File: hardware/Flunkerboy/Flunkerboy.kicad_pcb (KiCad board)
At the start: 2 copper layers, 51 x 60.4 mm, 23 parts, among them J1 GameBoy_GamePak_DMG-09, J2 Conn_01x01_Socket, J3 Conn_01x01_Socket, U1 74LS574, U2 74LS04, U5 AD9283, U6 OPA2333AIDR(UMW), U7 CD4051B

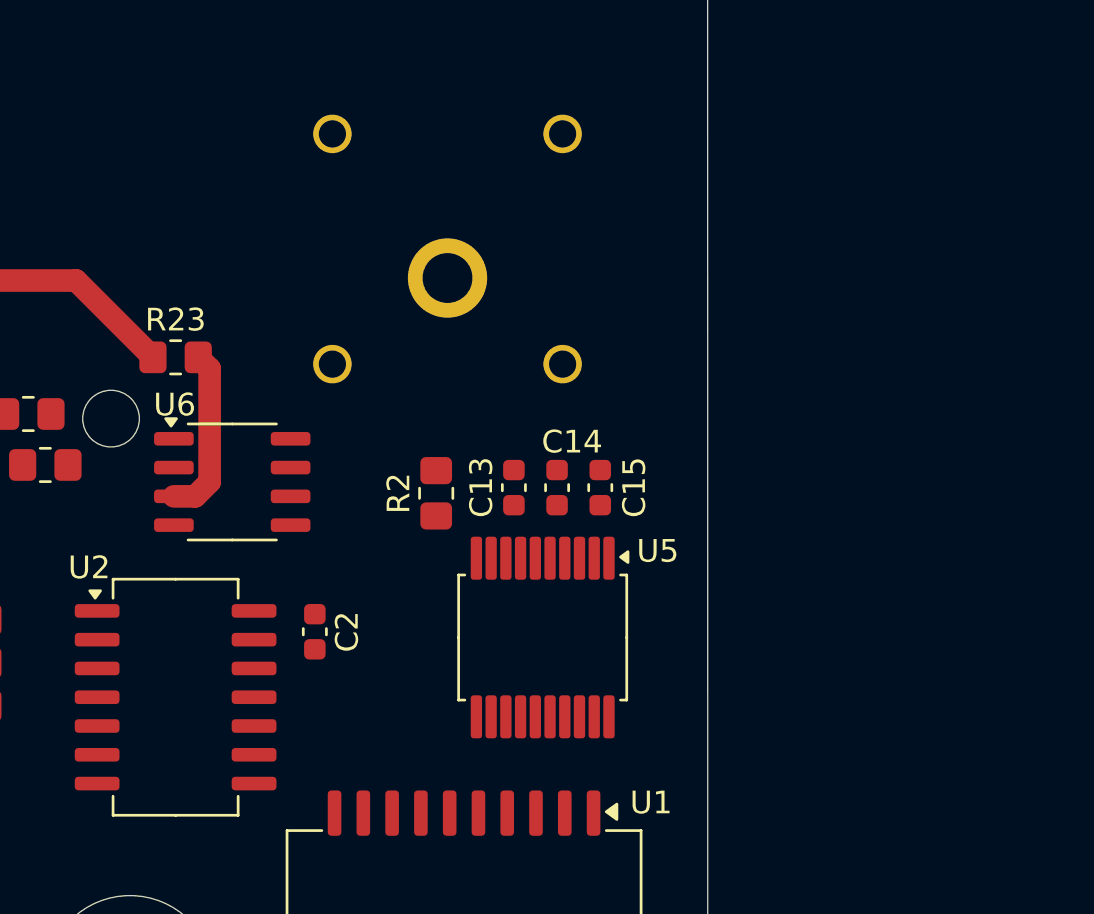
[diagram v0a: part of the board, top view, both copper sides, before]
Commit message: add mosfets
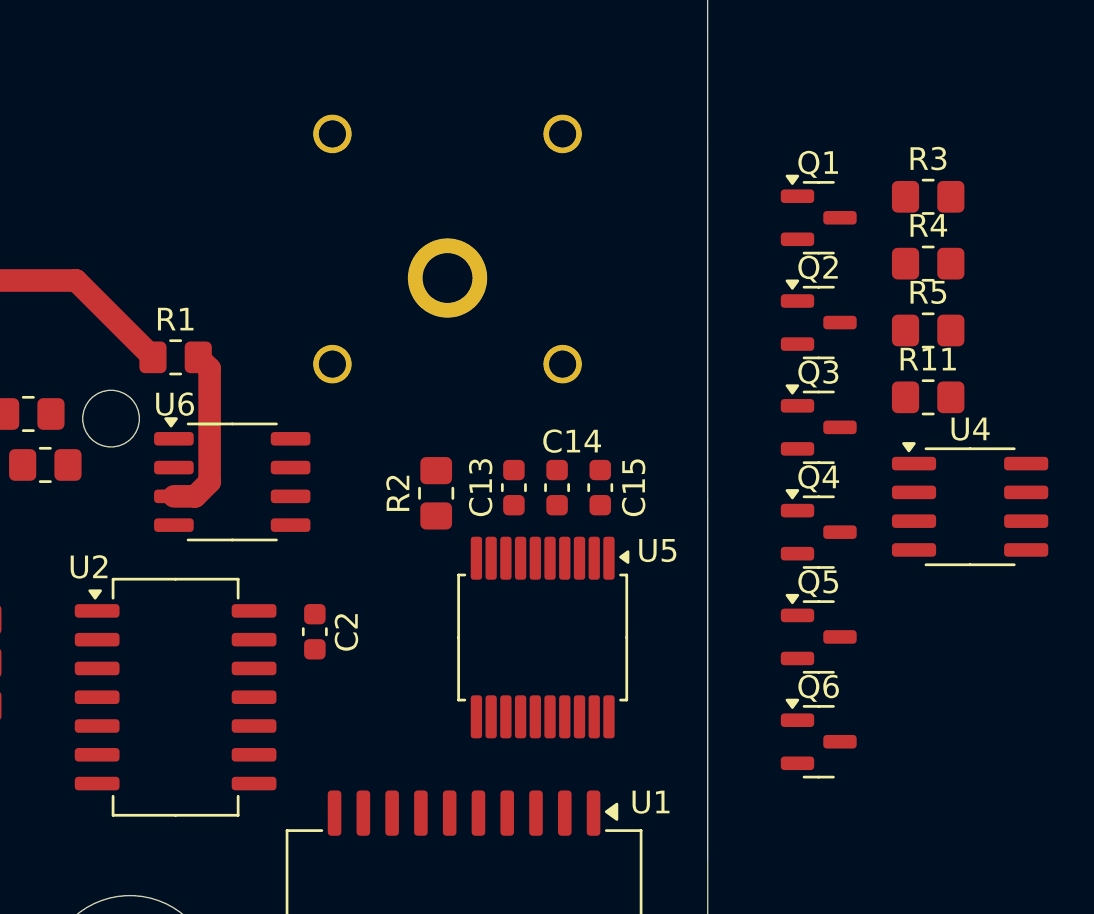
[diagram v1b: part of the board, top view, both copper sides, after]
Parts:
- added Q1: AO3400A, Package_TO_SOT_SMD:SOT-23, F.Cu at (129.6, 83.1)
- added Q2: AO3400A, Package_TO_SOT_SMD:SOT-23, F.Cu at (129.6, 87.7)
- added Q3: AO3400A, Package_TO_SOT_SMD:SOT-23, F.Cu at (129.6, 92.3)
- added Q4: AO3400A, Package_TO_SOT_SMD:SOT-23, F.Cu at (129.6, 97.0)
- added Q5: AO3400A, Package_TO_SOT_SMD:SOT-23, F.Cu at (129.6, 101.6)
- added Q6: AO3400A, Package_TO_SOT_SMD:SOT-23, F.Cu at (129.6, 106.2)
- added R11: 235k, Resistor_SMD:R_0805_2012Metric_Pad1.20x1.40mm_HandSolder, F.Cu at (134.4, 91.0)
- added R3: 235k, Resistor_SMD:R_0805_2012Metric_Pad1.20x1.40mm_HandSolder, F.Cu at (134.4, 82.2)
- added R4: 235k, Resistor_SMD:R_0805_2012Metric_Pad1.20x1.40mm_HandSolder, F.Cu at (134.4, 85.1)
- added R5: 235k, Resistor_SMD:R_0805_2012Metric_Pad1.20x1.40mm_HandSolder, F.Cu at (134.4, 88.1)
- added U4: OPA356xxD, Package_SO:SOIC-8_3.9x4.9mm_P1.27mm, F.Cu at (136.3, 95.8)
- R25: value 56k -> 55k
- renumbered R23 to R1
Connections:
- R1 pad 1: Net-(J2-Pin_1) -> /Vmes
- R1 pad 2: Net-(U6A-+) -> GND
- R10 pad 1: GND -> /Vmes
- R10 pad 2: Net-(U7-X5) -> Net-(Q6-S)
- R24 pad 2: Net-(U6A--) -> Net-(R11-Pad1)
- R25 pad 1: Net-(U6A--) -> Net-(R11-Pad1)
- R6 pad 1: GND -> /Vmes
- R6 pad 2: Net-(U7-X1) -> Net-(Q2-S)
- R7 pad 1: GND -> /Vmes
- R7 pad 2: Net-(U7-X2) -> Net-(Q3-S)
- R8 pad 1: GND -> /Vmes
- R8 pad 2: Net-(U7-X3) -> Net-(Q4-S)
- R9 pad 1: GND -> /Vmes
- R9 pad 2: Net-(U7-X4) -> Net-(Q5-S)
- U5 pad 5: +3.3V -> unconnected-(U5-VaD-Pad5)
- U5 pad 7: Ain -> unconnected-(U5-Ain+-Pad7)
- U5 pad 8: +3.3V -> unconnected-(U5-VaD-Pad8)
- U7 pad 1: Net-(U7-X4) -> Net-(Q5-G)
- U7 pad 12: Net-(U7-X3) -> Net-(Q4-G)
- U7 pad 13: GND -> Net-(Q1-G)
- U7 pad 14: Net-(U7-X1) -> /Vmes
- U7 pad 15: Net-(U7-X2) -> Net-(Q3-G)
- U7 pad 3: Net-(U6A-+) -> +3.3V
- U7 pad 5: Net-(U7-X5) -> Net-(Q6-G)

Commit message: build imput devider
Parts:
- removed Q1, Q2, Q3, Q4, Q5, Q6: AO3400A, Package_TO_SOT_SMD:SOT-23
- removed R9: 115k, Resistor_SMD:R_0805_2012Metric_Pad1.20x1.40mm_HandSolder
- removed U2: 74LS04, Package_SO:SO-14_5.3x10.2mm_P1.27mm
- added C10: C, Capacitor_SMD:C_0805_2012Metric, F.Cu at (167.2, 86.4)
- added C11: C, Capacitor_SMD:C_0805_2012Metric, F.Cu at (167.2, 89.5)
- added C16: 100n, Capacitor_SMD:C_0805_2012Metric, F.Cu at (167.2, 95.5)
- added C17: 100n, Capacitor_SMD:C_0805_2012Metric, F.Cu at (171.6, 86.4)
- added C18: 100n, Capacitor_SMD:C_0805_2012Metric, F.Cu at (171.6, 89.5)
- added C19: 100n, Capacitor_SMD:C_0805_2012Metric, F.Cu at (171.6, 92.5)
- added C20: 100n, Capacitor_SMD:C_0805_2012Metric, F.Cu at (171.6, 95.5)
- added C3: 100n, Capacitor_SMD:C_0805_2012Metric, F.Cu at (158.3, 89.5)
- added C4: 100n, Capacitor_SMD:C_0805_2012Metric, F.Cu at (158.3, 92.5)
- added C5: 100n, Capacitor_SMD:C_0805_2012Metric, F.Cu at (158.3, 95.5)
- added C6: 100n, Capacitor_SMD:C_0805_2012Metric, F.Cu at (162.7, 86.4)
- added C7: 100n, Capacitor_SMD:C_0805_2012Metric, F.Cu at (162.7, 89.5)
- added C8: 100n, Capacitor_SMD:C_0805_2012Metric, F.Cu at (162.7, 92.5)
- added C9: 100n, Capacitor_SMD:C_0805_2012Metric, F.Cu at (162.7, 95.5)
- added D1: 1N4007, Diode_SMD:D_SOD-123F, F.Cu at (158.8, 102.9)
- added D10: LM385, Package_TO_SOT_SMD:SOT-23, F.Cu at (145.3, 114.7)
- added D1a1: 1N4007, Diode_SMD:D_SOD-123F, F.Cu at (158.8, 109.6)
- added D2: 1N4007, Diode_SMD:D_SOD-123F, F.Cu at (158.8, 106.2)
- added D2a1: 1N4007, Diode_SMD:D_SOD-123F, F.Cu at (158.8, 113.0)
- added D3: 3.3V, Diode_SMD:D_SOD-123, F.Cu at (145.7, 107.3)
- added D4: 1V, Diode_SMD:D_SOD-123F, F.Cu at (196.2, 84.9)
- added D6: 8.2V 1.3W, Diode_SMD:D_SMB, F.Cu at (165.7, 104.0)
- added D7: 8,2V 1,3W, Diode_SMD:D_SMB, F.Cu at (165.7, 109.5)
- added D8: DX400, Diode_SMD:D_SOD-123, F.Cu at (151.1, 110.8)
- added D9: DX400, Diode_SMD:D_SOD-123, F.Cu at (145.7, 110.6)
- added F1: 2A, MyLibrary:2410, F.Cu at (166.3, 114.2)
- added F2: 50mA, Resistor_SMD:R_0805_2012Metric, F.Cu at (145.0, 86.4)
- added F3: 50mA, Resistor_SMD:R_0805_2012Metric, F.Cu at (145.0, 89.4)
- added K1: AGQ200A4HZ, Relay_THT:Relay_DPDT_Omron_G6K-2P-Y, F.Cu at (135.3, 75.4)
- added K2: AGQ200A4HZ, Relay_THT:Relay_DPDT_Omron_G6K-2P-Y, F.Cu at (143.7, 75.4)
- added K3: AGQ200A4HZ, Relay_THT:Relay_DPDT_Omron_G6K-2P-Y, F.Cu at (152.1, 75.4)
- added K4: AGQ200A4HZ, Relay_THT:Relay_DPDT_Omron_G6K-2P-Y, F.Cu at (160.4, 75.4)
- added R12: 235k, Resistor_SMD:R_0805_2012Metric_Pad1.20x1.40mm_HandSolder, F.Cu at (178.2, 80.6)
- added R13: 235k, Resistor_SMD:R_0805_2012Metric_Pad1.20x1.40mm_HandSolder, F.Cu at (178.2, 83.5)
- added R14: 25, Resistor_SMD:R_0805_2012Metric_Pad1.20x1.40mm_HandSolder, F.Cu at (178.2, 86.5)
- added R37: 2k2, Resistor_SMD:R_0805_2012Metric, F.Cu at (149.4, 95.3)
- added R39: 15k, Resistor_SMD:R_0805_2012Metric, F.Cu at (149.4, 98.2)
- added R40: 2k2, Resistor_SMD:R_0805_2012Metric, F.Cu at (149.4, 101.2)
- added R42: 10k, Resistor_SMD:R_0805_2012Metric, F.Cu at (149.4, 104.1)
- added R46: 100, Resistor_SMD:R_0805_2012Metric, F.Cu at (153.8, 86.4)
- added R47: 1k, Resistor_SMD:R_0805_2012Metric, F.Cu at (153.8, 89.4)
- added R63: 1k, Resistor_SMD:R_0805_2012Metric, F.Cu at (153.8, 92.3)
- added RV41: 100k, Resistor_SMD:R_0805_2012Metric, F.Cu at (153.8, 95.3)
- added U13: AD9283, Package_SO:SSOP-20_5.3x7.2mm_P0.65mm, F.Cu at (185.8, 94.5)
- added U14: 74LS574, Package_SO:SOIC-20W_7.5x15.4mm_P1.27mm, F.Cu at (187.0, 81.7)
- added U8: ADG1611, Package_SO:TSSOP-16_4.4x5mm_P0.65mm, F.Cu at (138.4, 114.6)
- C12, C2: footprint Capacitor_SMD:C_0603_1608Metric -> Capacitor_SMD:C_0805_2012Metric
- J2, J3: moved to F.Cu
- R1: value 5k -> 900k; footprint Resistor_SMD:R_0805_2012Metric_Pad1.20x1.40mm_HandSolder -> Resistor_SMD:R_0805_2012Metric
- R2: value 25 -> 90k; footprint Resistor_SMD:R_0805_2012Metric_Pad1.20x1.40mm_HandSolder -> Resistor_SMD:R_0805_2012Metric
- R3: value 235k -> 9k; footprint Resistor_SMD:R_0805_2012Metric_Pad1.20x1.40mm_HandSolder -> Resistor_SMD:R_0805_2012Metric
- R4: value 235k -> 900; footprint Resistor_SMD:R_0805_2012Metric_Pad1.20x1.40mm_HandSolder -> Resistor_SMD:R_0805_2012Metric
- R5: value 235k -> 90; footprint Resistor_SMD:R_0805_2012Metric_Pad1.20x1.40mm_HandSolder -> Resistor_SMD:R_0805_2012Metric
- R6: value 10k -> 9; footprint Resistor_SMD:R_0805_2012Metric_Pad1.20x1.40mm_HandSolder -> Resistor_SMD:R_0805_2012Metric
- R7: value 25k -> 0.9; footprint Resistor_SMD:R_0805_2012Metric_Pad1.20x1.40mm_HandSolder -> Resistor_SMD:R_0805_2012Metric
- R8: value 55k -> 0.1; footprint Resistor_SMD:R_0805_2012Metric_Pad1.20x1.40mm_HandSolder -> Resistor_SMD:R_0805_2012Metric
- U1: value 74LS574 -> OPA356xxD; footprint Package_SO:SOIC-20W_7.5x15.4mm_P1.27mm -> Package_SO:SOIC-8_3.9x4.9mm_P1.27mm
- U4: value OPA356xxD -> ADG1611; footprint Package_SO:SOIC-8_3.9x4.9mm_P1.27mm -> Package_SO:TSSOP-16_4.4x5mm_P0.65mm
- U5: value AD9283 -> ADG1611; footprint Package_SO:SSOP-20_5.3x7.2mm_P0.65mm -> Package_SO:TSSOP-16_4.4x5mm_P0.65mm
- U6: value OPA2333AIDR(UMW) -> ADG1611; footprint Package_SO:SO-8_3.9x4.9mm_P1.27mm -> Package_SO:TSSOP-16_4.4x5mm_P0.65mm
- U7: value CD4051B -> ADG1611; footprint Package_SO:SO-16_3.9x9.9mm_P1.27mm -> Package_SO:TSSOP-16_4.4x5mm_P0.65mm
- moved R10 102.4 mm to (178.2, 74.7)
- moved C1 85.8 mm to (195.4, 74.5)
- moved U1 83.9 mm to (195.3, 93.5), turned to 0 degrees
- moved R25 83.5 mm to (178.2, 92.4)
- moved R24 82.9 mm to (178.2, 89.4)
- moved C13 81.3 mm to (195.4, 77.0), turned to 0 degrees
- moved C14 78.9 mm to (195.4, 79.5), turned to 0 degrees
- moved C12 78.5 mm to (167.2, 92.5), turned to 0 degrees
- moved C15 76.6 mm to (195.4, 82.0), turned to 0 degrees
- moved R6 59.8 mm to (149.4, 86.4), turned to 0 degrees
- moved R8 58.8 mm to (149.4, 92.3), turned to 0 degrees
- moved R7 58.6 mm to (149.4, 89.4), turned to 0 degrees
- moved C2 53.0 mm to (158.3, 86.4), turned to 0 degrees
- moved U7 52.4 mm to (138.4, 108.0)
- moved R11 45.8 mm to (178.2, 77.6)
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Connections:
- net /SW3 renamed /Eingangsteiler/S10b
- net Ain renamed /Eingangsteiler/S8b
- C12 pad 1: +3.3V -> Net-(D3-K)
- C12 pad 2: GND -> /Eingangsteiler/D
- C13 pad 1: Net-(U5-Ain-) -> Net-(U13-Ain-)
- C15 pad 1: Net-(U5-VREFin) -> Net-(U13-VREFin)
- C2 pad 1: +3.3V -> -3V3
- J3 pad 1: GND -> GNDA
- R1 pad 1: /Vmes -> Net-(U5C-S3)
- R1 pad 2: GND -> Net-(U6C-S3)
- R10 pad 2: Net-(Q6-S) -> Net-(U1-+)
- R11 pad 2: Net-(U4--) -> Net-(U1--)
- R2 pad 1: Net-(U5-Ain-) -> Net-(U6C-S3)
- R2 pad 2: GND -> Net-(U4C-S3)
- R3 pad 1: Net-(U4-+) -> Net-(U4C-S3)
- R3 pad 2: GND -> Net-(U5B-S2)
- R4 pad 1: /Vmes -> Net-(U5B-S2)
- R4 pad 2: Net-(U4-+) -> Net-(U5A-S1)
- R5 pad 1: Net-(U4--) -> Net-(U5A-S1)
- R5 pad 2: Net-(R5-Pad2) -> Net-(U4B-S2)
- R6 pad 1: /Vmes -> Net-(U4B-S2)
- R6 pad 2: Net-(Q2-S) -> Net-(U4D-S4)
- R7 pad 1: /Vmes -> Net-(U4D-S4)
- R7 pad 2: Net-(Q3-S) -> Net-(U8B-S2)
- R8 pad 1: /Vmes -> Net-(U8B-S2)
- R8 pad 2: Net-(Q4-S) -> GNDA
- U1 pad 1: GND -> unconnected-(U1-NC-Pad1)
- U1 pad 2: Net-(U1-D0) -> Net-(U1--)
- U1 pad 3: Net-(U1-D1) -> Net-(U1-+)
- U1 pad 4: Net-(U1-D2) -> -3V3
- U1 pad 5: Net-(U1-D3) -> unconnected-(U1-NC-Pad5)
- U1 pad 6: Net-(U1-D4) -> Net-(R13-Pad2)
- U1 pad 7: Net-(U1-D5) -> +3.3V
- U1 pad 8: Net-(U1-D6) -> unconnected-(U1-NC-Pad8)
- U4 pad 1: unconnected-(U4-NC-Pad1) -> /Eingangsteiler/S6a
- U4 pad 2: Net-(U4--) -> Net-(D6-K)
- U4 pad 3: Net-(U4-+) -> Net-(U4A-S1)
- U4 pad 5: unconnected-(U4-NC-Pad5) -> GND
- U4 pad 6: Net-(R5-Pad2) -> Net-(U4D-S4)
- U4 pad 7: +3.3V -> Net-(U4D-D4)
- U4 pad 8: unconnected-(U4-NC-Pad8) -> /Eingangsteiler/S6e
- U5 pad 1: GND -> /Eingangsteiler/S7b
- U5 pad 10: /CLKadc -> Net-(U5C-D3)
- U5 pad 11: Net-(U1-D7) -> Net-(U5C-S3)
- U5 pad 12: Net-(U1-D6) -> unconnected-(U5E-NC-Pad12)
- U5 pad 13: Net-(U1-D5) -> +3V3
- U5 pad 14: Net-(U1-D4) -> Net-(U5B-S2)
- U5 pad 15: +3.3V -> Net-(D1-A)
- U5 pad 16: GND -> /Eingangsteiler/S7d
- U5 pad 2: Net-(U5-VREFin) -> Net-(U4B-D2)
- U5 pad 3: Net-(U5-VREFin) -> Net-(U5A-S1)
- U5 pad 4: GND -> -3V3
- U5 pad 5: unconnected-(U5-VaD-Pad5) -> GND
- U5 pad 6: Net-(U5-Ain-) -> Net-(U4A-S1)
- U5 pad 7: unconnected-(U5-Ain+-Pad7) -> Net-(D6-K)
- U5 pad 8: unconnected-(U5-VaD-Pad8) -> /Eingangsteiler/S7f
- U5 pad 9: GND -> /Eingangsteiler/S7e
- U6 pad 2: Net-(U6A--) -> Net-(U4B-D2)
- U6 pad 3: Net-(U6A-+) -> Net-(U5B-S2)
- U6 pad 4: (no net) -> -3V3
- U6 pad 5: (no net) -> GND
- U6 pad 6: (no net) -> Net-(U4C-S3)
- U6 pad 7: (no net) -> Net-(U4B-D2)
- U6 pad 8: (no net) -> /Eingangsteiler/S9b
- U7 pad 1: Net-(Q5-G) -> /Eingangsteiler/S9d
- U7 pad 10: /SW2 -> Net-(U4B-D2)
- U7 pad 11: /SW1 -> Net-(U6C-S3)
- U7 pad 12: Net-(Q4-G) -> unconnected-(U7E-NC-Pad12)
- U7 pad 13: Net-(Q1-G) -> +3V3
- U7 pad 14: /Vmes -> Net-(U4C-S3)
- U7 pad 15: Net-(Q3-G) -> Net-(U5C-D3)
- U7 pad 16: +3.3V -> /Eingangsteiler/S9e
- U7 pad 2: unconnected-(U7-X6-Pad2) -> Net-(D1-A)
- U7 pad 3: +3.3V -> Net-(U4B-S2)
- U7 pad 4: unconnected-(U7-X7-Pad4) -> -3V3
- U7 pad 5: Net-(Q6-G) -> GND
- U7 pad 6: GND -> Net-(U4D-S4)
- U7 pad 7: GND -> Net-(D1-A)
- U7 pad 8: GND -> /Eingangsteiler/S10d
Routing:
- net Net-(J2-Pin_1): track 16.4 -> 0.00 mm
- net Net-(U6A-+): track 7.55 -> 0.00 mm
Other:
- outline, holes or cut-outs redrawn
- board text added: "32"

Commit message: add docs
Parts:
- removed C17, C18, C19, C20: 100n, Capacitor_SMD:C_0805_2012Metric
- removed K1, K2, K3, K4: AGQ200A4HZ, Relay_THT:Relay_DPDT_Omron_G6K-2P-Y
- added D11: 1N4148, Diode_SMD:D_SOD-123, F.Cu at (77.6, 73.2)
- added D12: 1N4148, Diode_SMD:D_SOD-123, F.Cu at (120.6, 73.5)
- added D13: 1N4148, Diode_SMD:D_SOD-123, F.Cu at (114.3, 94.7)
- added D5: 1N4148, Diode_SMD:D_SOD-123, F.Cu at (76.2, 96.9)
- added RL1: AGQ200A4HZ, Relay_THT:Relay_DPDT_Omron_G6K-2P-Y, F.Cu at (80.3, 94.1)
- added RL3: AGQ200A4HZ, Relay_THT:Relay_DPDT_Omron_G6K-2P-Y, F.Cu at (123.2, 94.7)
- added RL4: AGQ200A4HZ, Relay_THT:Relay_DPDT_Omron_G6K-2P-Y, F.Cu at (118.1, 76.5)
- added RL6: AGQ200A4HZ, Relay_THT:Relay_DPDT_Omron_G6K-2P-Y, F.Cu at (74.9, 75.8)
- RV41: footprint Resistor_SMD:R_0805_2012Metric -> Potentiometer_SMD:Potentiometer_Bourns_3224J_Horizontal
- moved C16 112.5 mm to (56.9, 117.5)
- moved RV41 99.0 mm to (56.4, 113.2)
- moved R40 98.8 mm to (51.1, 111.3)
- moved D8 97.2 mm to (54.1, 105.0)
- moved F2 95.9 mm to (51.4, 107.2)
- moved C15 94.9 mm to (103.1, 104.3)
- moved C13 94.1 mm to (104.1, 99.5)
- moved D10 94.0 mm to (51.2, 115.2)
- moved R39 87.1 mm to (63.2, 111.0)
- moved R42 87.1 mm to (63.2, 117.0)
- moved C2 87.1 mm to (103.2, 153.9)
- moved C3 87.1 mm to (103.2, 156.9)
- moved D9 86.2 mm to (59.8, 104.8)
- moved D4 86.1 mm to (110.9, 97.5), turned to 180 degrees
- moved C1 84.1 mm to (122.2, 116.0)
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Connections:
- R13 pad 2: Net-(R13-Pad2) -> Net-(U13-Ain+)
- U1 pad 6: Net-(R13-Pad2) -> Net-(U13-Ain+)
- U13 pad 7: unconnected-(U13-Ain+-Pad7) -> Net-(U13-Ain+)
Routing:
- added copper zone on B.Cu, net GND
- added copper zone on F.Cu, net GND

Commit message: add 3D files
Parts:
- moved U8 4.74 mm to (94.5, 95.7)
- moved C12 3.75 mm to (95.7, 90.7), turned to 0 degrees
- moved R37 1.76 mm to (95.0, 87.9)
- moved C11 0.95 mm to (98.4, 99.6), turned to 90 degrees
- moved D3 0.37 mm to (92.7, 88.6)
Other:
- outline, holes or cut-outs redrawn
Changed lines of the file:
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@@
 	(footprint "Capacitor_SMD:C_0805_2012Metric"
 		(layer "F.Cu")
-		(at 97.45 99.5825 -90)
+		(at 98.4 99.6 90)
 		(descr "Capacitor SMD 0805 (2012 Metric), square (rectangular) end terminal, IPC-7351 nominal, (Body size source: IPC-SM-782 page 76, https://www.pcb-3d.com/wordpress/wp-content/uploads/ipc-sm-782a_amendment_1_and_2.pdf, https://docs.google.com/spreadsheets/d/1BsfQQcO9C6DZCsRaXUlFlo91Tg2WpOkGARC1WS5S8t0/edit?usp=sharing), generated with kicad-footprint-generator")
 		(tags "capacitor")
@@
 		(attr smd)
 		(fp_line
-			(start -0.261253 0.735)
-			(end 0.261253 0.735)
+			(start -0.261253 -0.735)
+			(end 0.261253 -0.735)
 			(stroke
 				(width 0.12)
@@
 		)
 		(fp_line
-			(start -0.261253 -0.735)
-			(end 0.261253 -0.735)
+			(start -0.261253 0.735)
+			(end 0.261253 0.735)
 			(stroke
 				(width 0.12)
@@
 		)
 		(fp_line
-			(start -1.7 0.98)
-			(end -1.7 -0.98)
+			(start 1.7 -0.98)
+			(end 1.7 0.98)
 			(stroke
 				(width 0.05)
@@
 		)
 		(fp_line
-			(start 1.7 0.98)
-			(end -1.7 0.98)
+			(start -1.7 -0.98)
+			(end 1.7 -0.98)
 			(stroke
 				(width 0.05)
@@
 		)
 		(fp_line
-			(start -1.7 -0.98)
-			(end 1.7 -0.98)
+			(start 1.7 0.98)
+			(end -1.7 0.98)
 			(stroke
 				(width 0.05)
@@
 		)
 		(fp_line
-			(start 1.7 -0.98)
-			(end 1.7 0.98)
+			(start -1.7 0.98)
+			(end -1.7 -0.98)
 			(stroke
 				(width 0.05)
@@
 		)
 		(fp_line
-			(start -1 0.625)
-			(end -1 -0.625)
+			(start 1 -0.625)
+			(end 1 0.625)
 			(stroke
 				(width 0.1)
@@
 		)
 		(fp_line
-			(start 1 0.625)
-			(end -1 0.625)
+			(start -1 -0.625)
+			(end 1 -0.625)
 			(stroke
 				(width 0.1)
@@
 		)
 		(fp_line
-			(start -1 -0.625)
-			(end 1 -0.625)
+			(start 1 0.625)
+			(end -1 0.625)
 			(stroke
 				(width 0.1)
@@
 		)
 		(fp_line
-			(start 1 -0.625)
-			(end 1 0.625)
+			(start -1 0.625)
+			(end -1 -0.625)
 			(stroke
 				(width 0.1)
@@
 		)
 		(pad "1" smd roundrect
-			(at -0.949999 0 270)
+			(at -0.949999 0 90)
 			(size 1 1.45)
 			(layers "F.Cu" "F.Mask" "F.Paste")
@@
 		)
 		(pad "2" smd roundrect
-			(at 0.949999 0 270)
+			(at 0.949999 0 90)
 			(size 1 1.45)
 			(layers "F.Cu" "F.Mask" "F.Paste")
@@
 	(footprint "Package_SO:TSSOP-16_4.4x5mm_P0.65mm"
 		(layer "F.Cu")
-		(at 98.775 93.6375 -90)
+		(at 94.5 95.6875 -90)
 		(descr "TSSOP, 16 Pin (https://www.jedec.org/document_search?search_api_views_fulltext=MO-153), generated with kicad-footprint-generator ipc_gullwing_generator.py")
 		(tags "TSSOP SO JEDEC-MO-153-AB Texas_PW0016A Microchip-ST Toshiba-TSSOP16-P-0044-0.65A NXP-SOT403-1 Infineon-P-TSSOP-16-800")
@@
 		)
 		(embedded_fonts no)
+		(model "/home/jsc69/Dokumente/projekte/ComponentTester/3d/cartridge-back.step"
+			(offset
+				(xyz -29.5 -1 -3)
+			)
+			(scale
+				(xyz 1 1 1)
+			)
+			(rotate
+				(xyz -0 -0 -0)
+			)
+		)
+		(model "/home/jsc69/Dokumente/projekte/ComponentTester/3d/cartridge-front.step"
+			(hide yes)
+			(offset
+				(xyz -29.5 -1 4)
+			)
+			(scale
+				(xyz 1 1 1)
+			)
+			(rotate
+				(xyz -0 -180 -0)
+			)
+		)
 	)
 	(footprint "MyLibrary:2410"
@@
 	(footprint "Capacitor_SMD:C_0805_2012Metric"
 		(layer "F.Cu")
-		(at 92.868 93.16 -90)
+		(at 95.7 90.7)
 		(descr "Capacitor SMD 0805 (2012 Metric), square (rectangular) end terminal, IPC-7351 nominal, (Body size source: IPC-SM-782 page 76, https://www.pcb-3d.com/wordpress/wp-content/uploads/ipc-sm-782a_amendment_1_and_2.pdf, https://docs.google.com/spreadsheets/d/1BsfQQcO9C6DZCsRaXUlFlo91Tg2WpOkGARC1WS5S8t0/edit?usp=sharing), generated with kicad-footprint-generator")
 		(tags "capacitor")
 		(property "Reference" "C12"
-			(at 0 -1.679999 90)
+			(at 0 -1.679999 0)
 			(layer "F.SilkS")
 			(effects
@@
 		)
 		(property "Value" "100n"
-			(at 0 1.679999 90)
+			(at 0 1.679999 0)
 			(layer "F.Fab")
 			(effects
@@
 		)
 		(property "Datasheet" "~"
-			(at 0 0 90)
+			(at 0 0 0)
 			(layer "F.Fab")
 			(hide yes)
@@
 		)
 		(property "Description" "Unpolarized capacitor"
-			(at 0 0 90)
+			(at 0 0 0)
 			(layer "F.Fab")
 			(hide yes)
@@
 		(attr smd)
 		(fp_line
-			(start -0.261253 0.735)
-			(end 0.261253 0.735)
+			(start -0.261253 -0.735)
+			(end 0.261253 -0.735)
 			(stroke
 				(width 0.12)
@@
 		)
 		(fp_line
-			(start -0.261253 -0.735)
-			(end 0.261253 -0.735)
+			(start -0.261253 0.735)
+			(end 0.261253 0.735)
 			(stroke
 				(width 0.12)
@@
 		)
 		(fp_line
-			(start -1.7 0.98)
-			(end -1.7 -0.98)
+			(start -1.7 -0.98)
+			(end 1.7 -0.98)
 			(stroke
 				(width 0.05)
@@
 		)
 		(fp_line
-			(start 1.7 0.98)
-			(end -1.7 0.98)
+			(start -1.7 0.98)
+			(end -1.7 -0.98)
 			(stroke
 				(width 0.05)
@@
 		)
 		(fp_line
-			(start -1.7 -0.98)
-			(end 1.7 -0.98)
+			(start 1.7 -0.98)
+			(end 1.7 0.98)
 			(stroke
 				(width 0.05)
@@
 		)
 		(fp_line
-			(start 1.7 -0.98)
-			(end 1.7 0.98)
+			(start 1.7 0.98)
+			(end -1.7 0.98)
 			(stroke
 				(width 0.05)
@@
 		)
 		(fp_line
-			(start -1 0.625)
-			(end -1 -0.625)
+			(start -1 -0.625)
+			(end 1 -0.625)
 			(stroke
 				(width 0.1)
@@
 		)
 		(fp_line
-			(start 1 0.625)
-			(end -1 0.625)
+			(start -1 0.625)
+			(end -1 -0.625)
 			(stroke
 				(width 0.1)
@@
 		)
 		(fp_line
-			(start -1 -0.625)
-			(end 1 -0.625)
+			(start 1 -0.625)
+			(end 1 0.625)
 			(stroke
 				(width 0.1)
@@
 		)
 		(fp_line
-			(start 1 -0.625)
-			(end 1 0.625)
+			(start 1 0.625)
+			(end -1 0.625)
 			(stroke
 				(width 0.1)
@@
 		)
 		(fp_text user "${REFERENCE}"
-			(at 0 0 90)
+			(at 0 0 0)
 			(layer "F.Fab")
 			(effects
@@
 		)
 		(pad "1" smd roundrect
-			(at -0.949999 0 270)
+			(at -0.949999 0)
 			(size 1 1.45)
 			(layers "F.Cu" "F.Mask" "F.Paste")
@@
 		)
 		(pad "2" smd roundrect
-			(at 0.949999 0 270)
+			(at 0.949999 0)
 			(size 1 1.45)
 			(layers "F.Cu" "F.Mask" "F.Paste")
@@
 	(footprint "Diode_SMD:D_SOD-123"
 		(layer "F.Cu")
-		(at 92.71 88.97 90)
+		(at 92.71 88.6 90)
 		(descr "SOD-123")
 		(tags "SOD-123")
@@
 	(footprint "Resistor_SMD:R_0805_2012Metric"
 		(layer "F.Cu")
-		(at 94.996 89.662 -90)
+		(at 95 87.9 -90)
 		(descr "Resistor SMD 0805 (2012 Metric), square (rectangular) end terminal, IPC-7351 nominal, (Body size source: IPC-SM-782 page 72, https://www.pcb-3d.com/wordpress/wp-content/uploads/ipc-sm-782a_amendment_1_and_2.pdf), generated with kicad-footprint-generator")
 		(tags "resistor")
@@
 		(layer "Edge.Cuts")
 	)
+	(gr_circle
+		(center 99.1985 91.6)
+		(end 100.25 91.645)
+		(stroke
+			(width 0.05)
+			(type solid)
+		)
+		(fill no)
+		(layer "Edge.Cuts")
+	)
